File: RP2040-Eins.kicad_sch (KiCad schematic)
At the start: 50 parts, among them J1 Barrel_Jack_Switch, J2 CONN_I, J3 CONN_A, J4 CONN_P, J5 CONN_X, J6 USB_B_Micro, J7 CONN_JTAG, J8 CONN_D1, J9 CONN_D2, Q1 AO3401A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

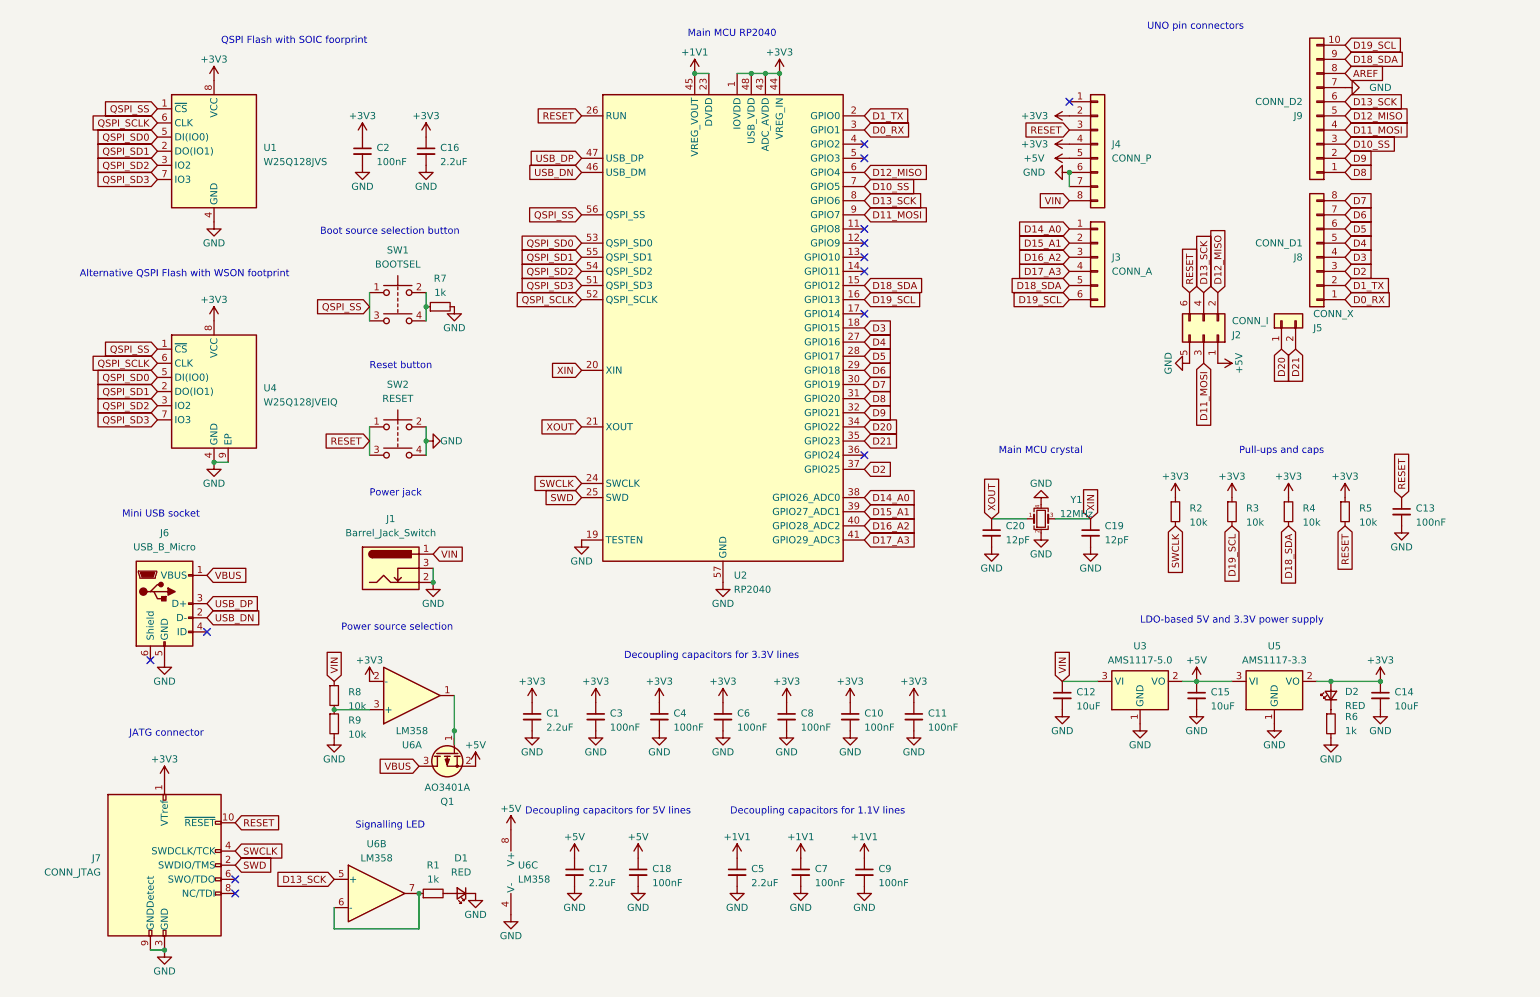
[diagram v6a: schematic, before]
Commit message: Switched to USB-C with all stuff around it.
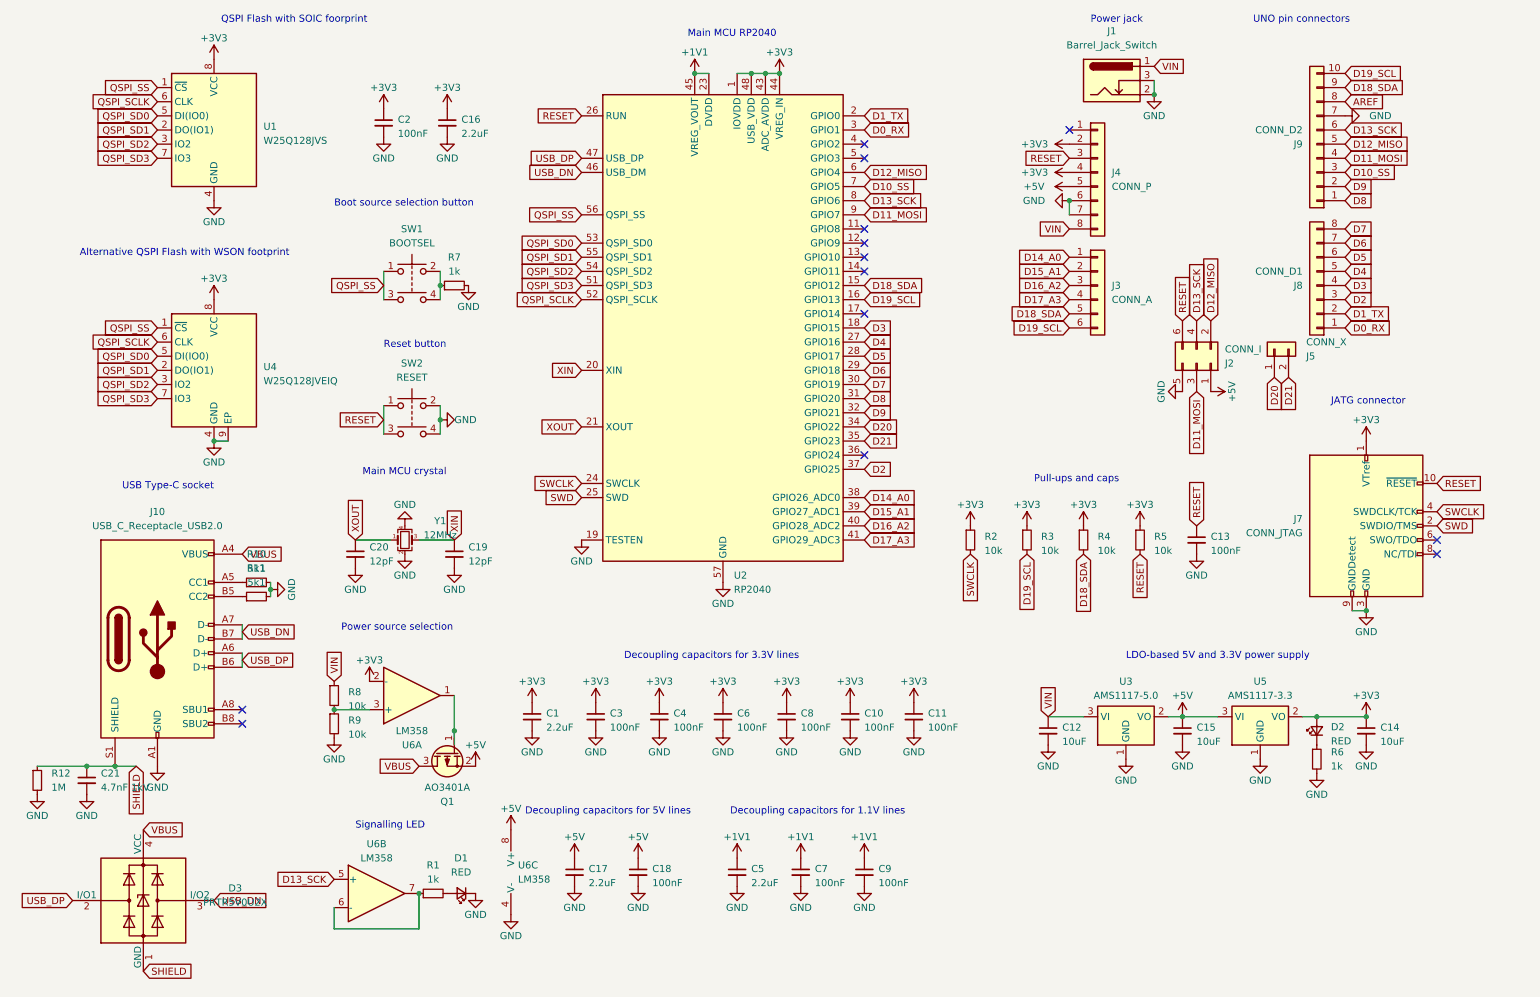
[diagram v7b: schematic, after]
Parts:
- removed J6: USB_B_Micro, Connector_USB:USB_Micro-B_Molex_47346-0001, symbol Connector:USB_B_Micro
- added C21: 4.7nF 1kV, Capacitor_SMD:C_1206_3216Metric, symbol Device:C_Small
- added D3: PRTR5V0U2X, Package_TO_SOT_SMD:SOT-143, symbol Power_Protection:PRTR5V0U2X
- added J10: USB_C_Receptacle_USB2.0, Connector_USB:USB_C_Receptacle_HRO_TYPE-C-31-M-12, symbol Connector:USB_C_Receptacle_USB2.0
- added R10, R11: 5k1, Resistor_SMD:R_0402_1005Metric, symbol Device:R_Small
- added R12: 1M, Resistor_SMD:R_0603_1608Metric, symbol Device:R_Small
- J2: footprint Connector_PinSocket_2.54mm:PinSocket_2x03_P2.54mm_Vertical -> Connector_PinHeader_2.54mm:PinHeader_2x03_P2.54mm_Vertical
- J5: footprint Connector_PinSocket_2.54mm:PinSocket_1x02_P2.54mm_Vertical -> Connector_PinHeader_2.54mm:PinHeader_1x02_P2.54mm_Vertical
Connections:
- net GND: now also C21.2, J10.A1 (GND), J10.A12 (GND), J10.B1 (GND), J10.B12 (GND), R10.2, R11.2, R12.2
- net USB_DN: now also D3.3 (I/O2), J10.A7 (D-), J10.B7 (D-)
- net USB_DP: now also D3.2 (I/O1), J10.A6 (D+), J10.B6 (D+)
- net VBUS: now also D3.4 (VCC), J10.A4 (VBUS), J10.A9 (VBUS), J10.B4 (VBUS), J10.B9 (VBUS)
- new net: J10.A5 (CC1), R10.1
- new net: J10.B5 (CC2), R11.1
- new net SHIELD: C21.1, D3.1 (GND), J10.S1 (SHIELD), R12.1
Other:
- note added: "USB Type-C socket"
- note removed: "Mini USB socket"
- moved on the sheet: C12, C13, C14, C15, C16, C19, C2, C20, D2, J1, J2, J3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

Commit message: Moved stuff around
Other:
- moved on the sheet: C12, C14, C15, D2, J1, R6, U3, U5
